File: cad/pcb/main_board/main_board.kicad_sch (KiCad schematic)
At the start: 1 part, among them J1 USB_B_Micro

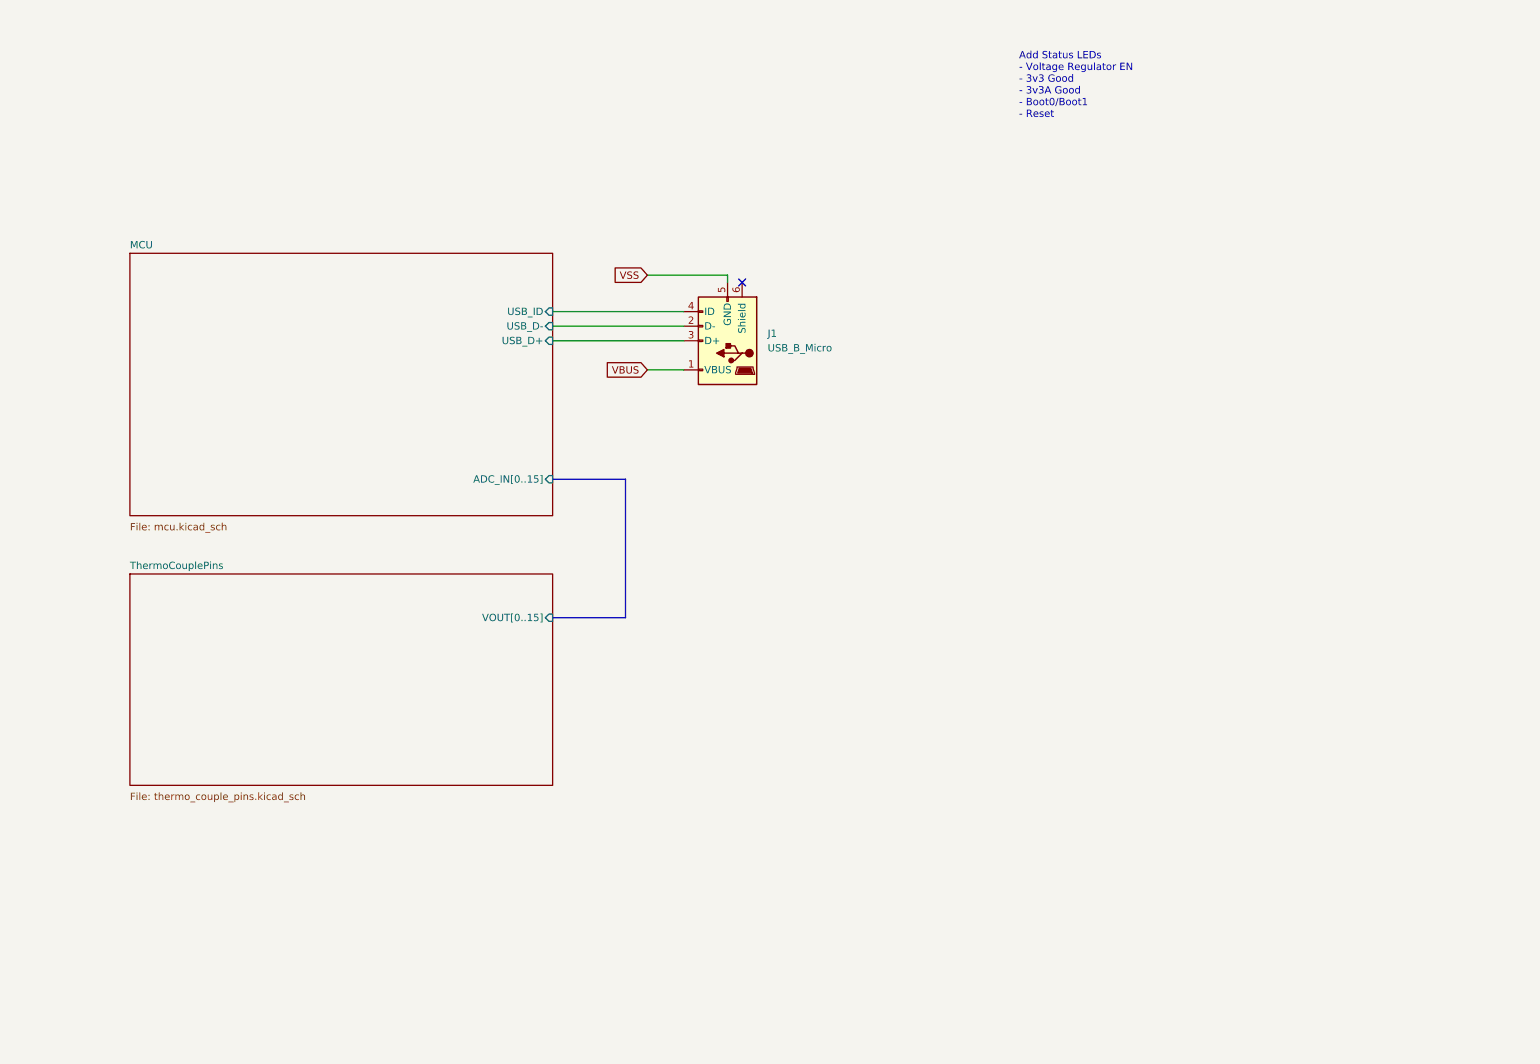
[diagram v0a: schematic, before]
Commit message: SWD connector start
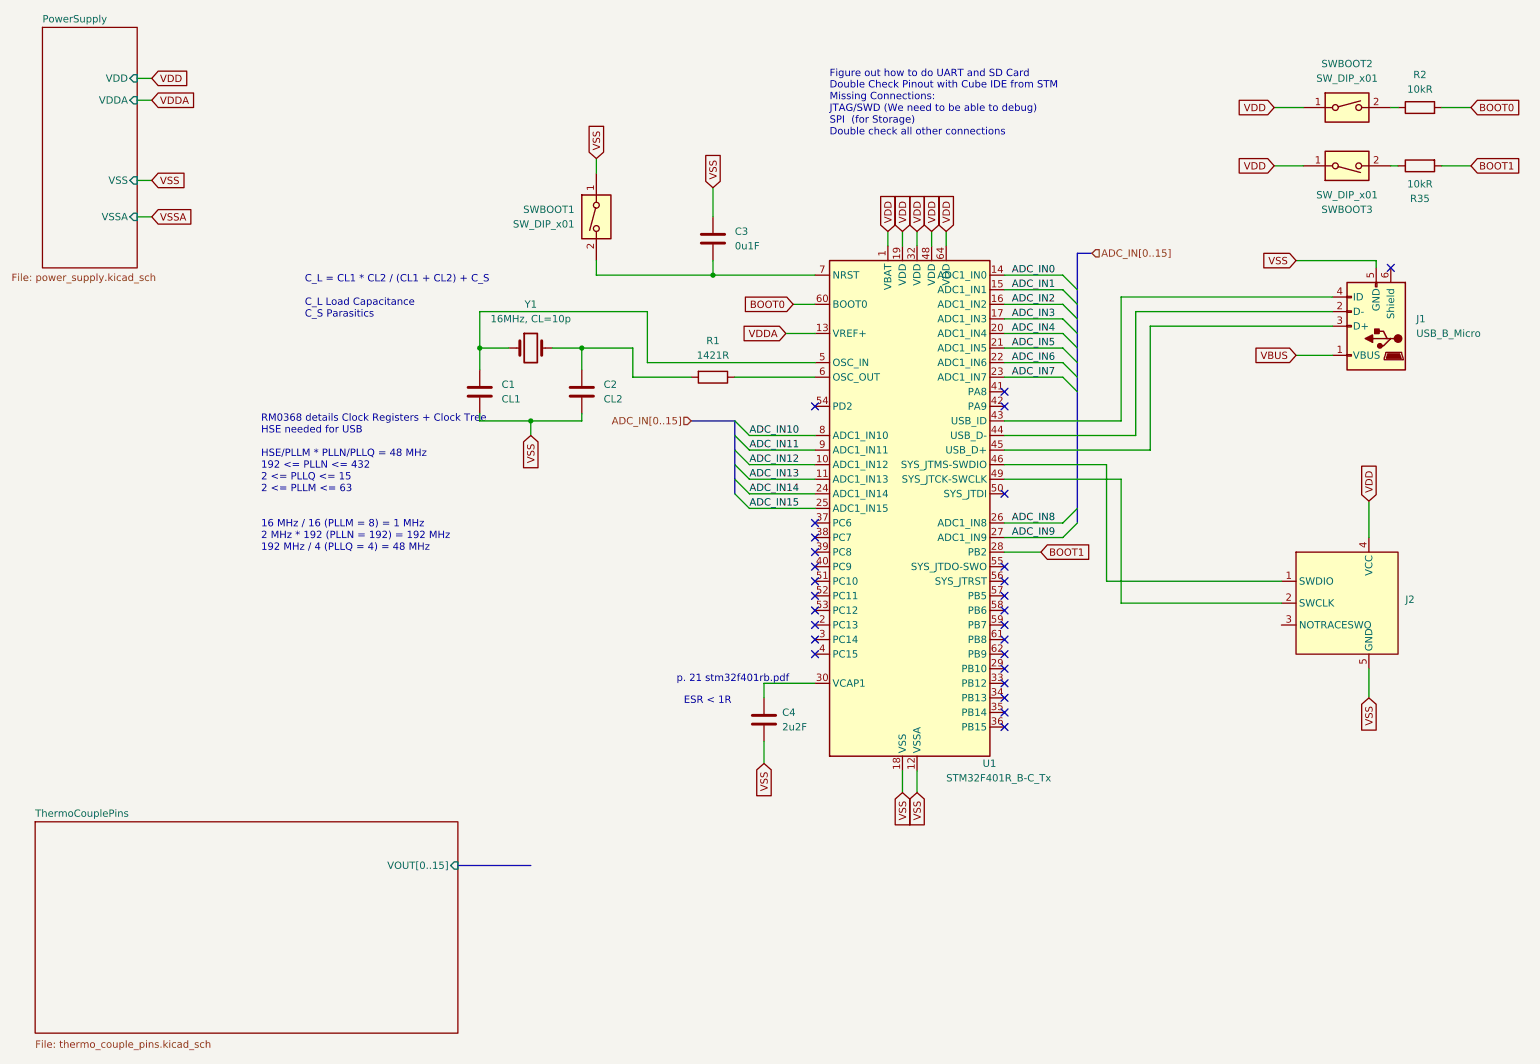
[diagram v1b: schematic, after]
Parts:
- added C1: CL1, Capacitor_SMD:C_0805_2012Metric, symbol Device:C
- added C2: CL2, Capacitor_SMD:C_0805_2012Metric, symbol Device:C
- added C3: 0u1F, Capacitor_SMD:C_0805_2012Metric, symbol Device:C
- added C4: 2u2F, Capacitor_SMD:C_0805_2012Metric, symbol Device:C
- added J2: ~, symbol local:SWD_Pogo
- added R1: 1421R, Resistor_SMD:R_0805_2012Metric, symbol Device:R
- added R2, R35: 10kR, Resistor_SMD:R_0805_2012Metric, symbol Device:R
- added SWBOOT1, SWBOOT2, SWBOOT3: SW_DIP_x01, Button_Switch_SMD:SW_DIP_SPSTx01_Slide_6.7x4.1mm_W6.73mm_P2.54mm_LowProfile_JPin, symbol Switch:SW_DIP_x01
- added U1: STM32F401R_B-C_Tx, Package_QFP:LQFP-64_10x10mm_P0.5mm, symbol MCU_ST_STM32F4:STM32F401R_B-C_Tx
- added Y1: 16MHz, CL=10p, local:FC4SDCBMF8.0-T1, symbol Device:Crystal
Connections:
- net VSS: now also C1.2, C2.2, C3.1, C4.2, J2.5 (GND), SWBOOT1.1, U1.12 (VSSA), U1.18 (VSS), U1.31 (VSS), U1.47 (VSS), U1.63 (VSS)
- net MCU/USB_D+: no longer names the net of J1.3 (D+)
- net MCU/USB_D+: now also U1.45 (PA12)
- net MCU/USB_D-: no longer names the net of J1.2 (D-)
- net MCU/USB_D-: now also U1.44 (PA11)
- net MCU/USB_ID: no longer names the net of J1.4 (ID)
- net MCU/USB_ID: now also U1.43 (PA10)
- new net: C3.2, SWBOOT1.2, U1.7 (NRST)
- new net: C2.1, R1.2, Y1.2
- new net: R35.1, SWBOOT3.2
- new net: C1.1, U1.5 (PH0), Y1.1
- new net: R2.1, SWBOOT2.2
- new net: J2.1 (SWDIO), U1.46 (PA13)
- new net: J2.2 (SWCLK), U1.49 (PA14)
- new net: C4.1, U1.30 (VCAP1)
- new net: R1.1, U1.6 (PH1)
- new net ADC_IN0: U1.14 (PA0)
- new net ADC_IN1: U1.15 (PA1)
- new net ADC_IN10: U1.8 (PC0)
- new net ADC_IN11: U1.9 (PC1)
- new net ADC_IN12: U1.10 (PC2)
- new net ADC_IN13: U1.11 (PC3)
- new net ADC_IN14: U1.24 (PC4)
- new net ADC_IN15: U1.25 (PC5)
- new net ADC_IN2: U1.16 (PA2)
- new net ADC_IN3: U1.17 (PA3)
- new net ADC_IN4: U1.20 (PA4)
- new net ADC_IN5: U1.21 (PA5)
- new net ADC_IN6: U1.22 (PA6)
- new net ADC_IN7: U1.23 (PA7)
- new net ADC_IN8: U1.26 (PB0)
- new net ADC_IN9: U1.27 (PB1)
- new net BOOT0: R2.2, U1.60 (BOOT0)
- new net BOOT1: R35.2, U1.28 (PB2)
- new net VDD: J2.4 (VCC), SWBOOT2.1, SWBOOT3.1, U1.1 (VBAT), U1.19 (VDD), U1.32 (VDD), U1.48 (VDD), U1.64 (VDD)
- new net VDDA: U1.13 (VREF+)
- no-connect marks 1 -> 27
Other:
- removed sheet MCU
- added sheet PowerSupply (power_supply.kicad_sch)
- note added: "C_L = CL1 * CL2 / (CL1 + CL2) + C_S C_L Load Capacitance C_S Parasitics"
- note added: "Double Check Pinout with Cube IDE from STM Missing Connections: JTAG/SWD (We need to be able to debug) SPI (for Storage) Double check all other connections"
- note added: "ESR < 1R"
- note added: "Figure out how to do UART and SD Card"
- note added: "RM0368 details Clock Registers + Clock Tree HSE needed for USB HSE/PLLM * PLLN/PLLQ = 48 MHz 192 <= PLLN <= 432 2 <= PLLQ <= 15 2 <= PLLM <= 63 16 MHz / 16 (PLLM = 8) = 1 MHz 2 MHz * 192 (PLLN = 192) = 192 MHz 192 MHz / 4 (PLLQ = 4) = 48 MHz"
- note added: "p. 21 stm32f401rb.pdf"
- note removed: "Add Status LEDs - Voltage Regulator EN - 3v3 Good - 3v3A Good - Boot0/Boot1 - Reset"
- moved on the sheet: J1
